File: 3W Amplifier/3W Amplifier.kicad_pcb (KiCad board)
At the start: 2 copper layers, 20 parts, among them SW1 SW_DIP_x02, U1 PAM8008

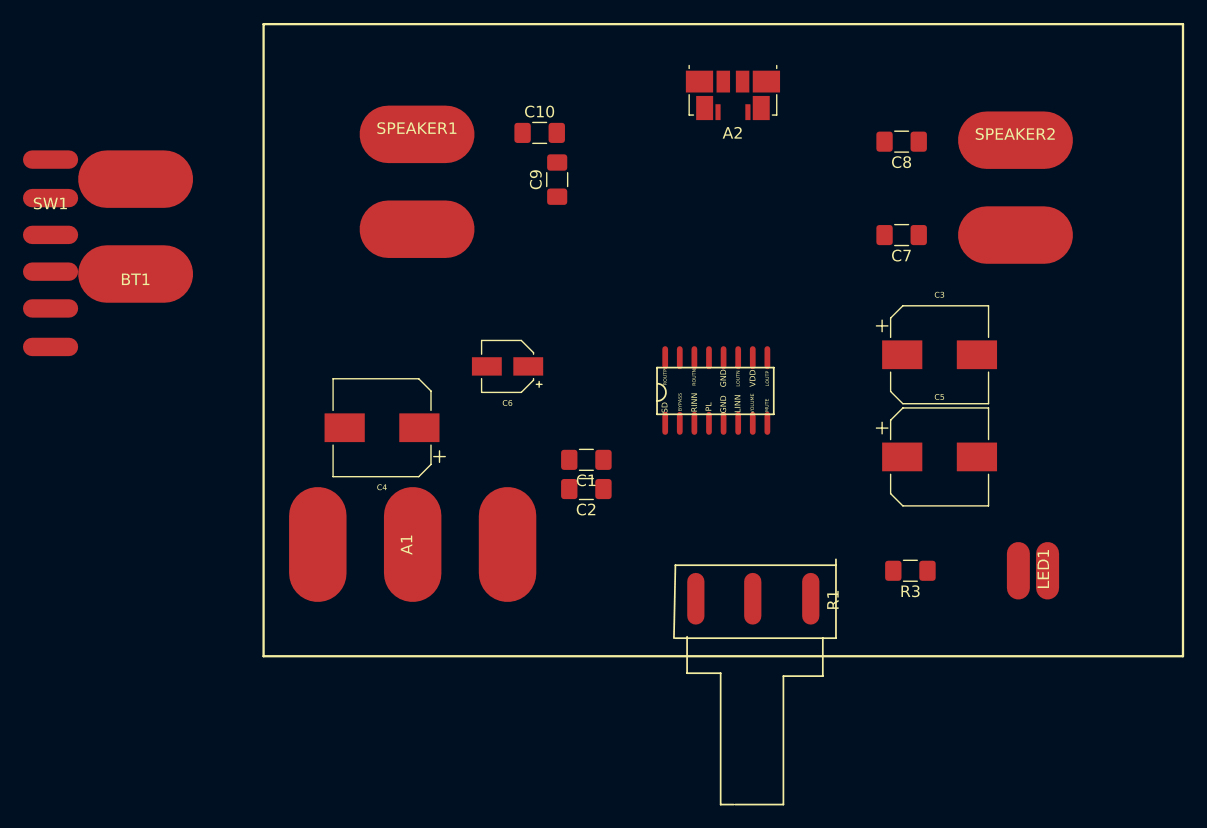
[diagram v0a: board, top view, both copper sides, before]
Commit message: everything routed but power
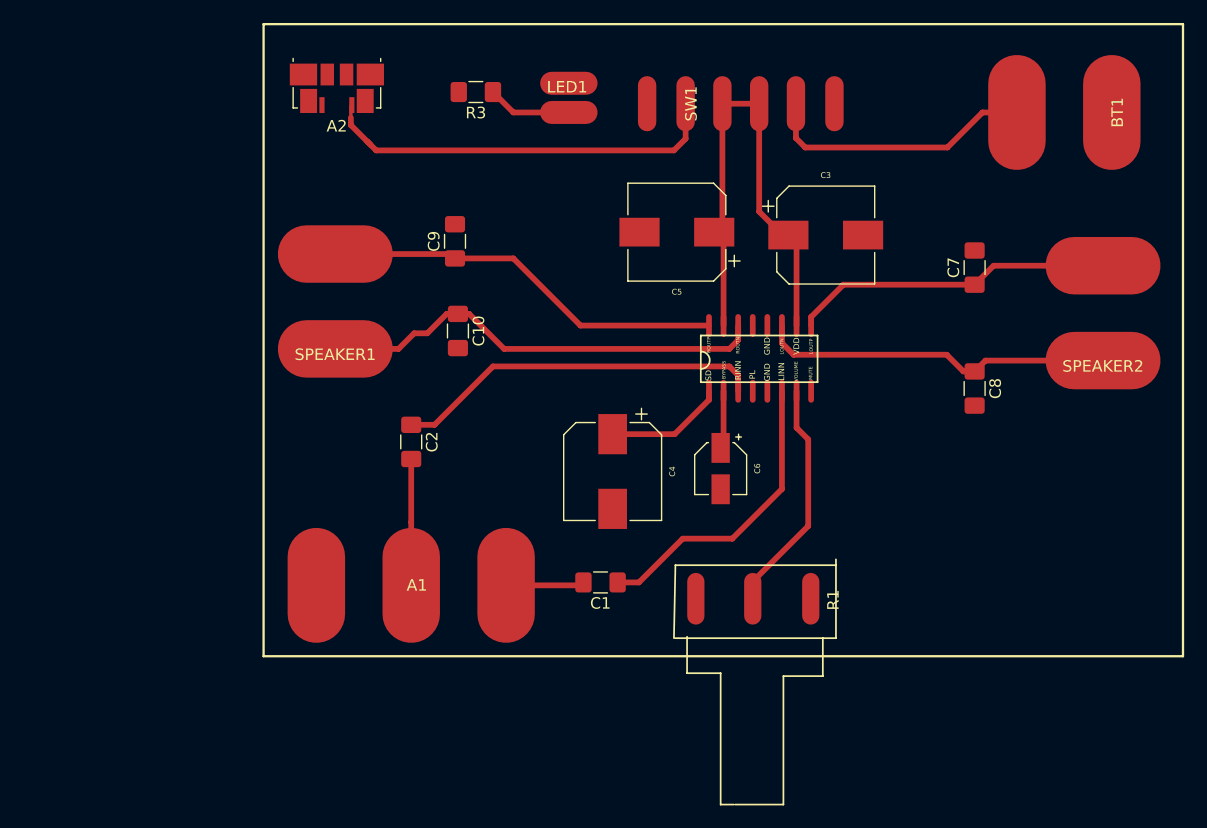
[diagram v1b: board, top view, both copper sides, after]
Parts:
- moved BT1 86.1 mm to (98.8, 27.7), turned to 90 degrees
- moved R3 56.3 mm to (43.5, 25.9)
- moved SW1 55.9 mm to (61.7, 26.9), turned to 90 degrees
- moved LED1 55.9 mm to (51.6, 27.7), turned to 0 degrees
- moved A2 34.5 mm to (31.4, 25.6)
- moved C5 30.1 mm to (61.0, 38.1), turned to 180 degrees
- moved C8 22.4 mm to (86.9, 51.7), turned to 270 degrees
- moved SPEAKER2 20.6 mm to (98.0, 49.3), turned to 0 degrees
- moved C6 20.6 mm to (64.8, 58.7), turned to 270 degrees
- moved C4 20.4 mm to (55.4, 58.9), turned to 270 degrees
- moved SPEAKER1 20.0 mm to (31.2, 48.3), turned to 0 degrees
- moved C10 18.6 mm to (41.9, 46.7), turned to 270 degrees
- moved C2 15.8 mm to (37.8, 56.4), turned to 270 degrees
- moved C3 14.4 mm to (73.9, 38.4)
- moved C1 10.7 mm to (54.3, 68.6)
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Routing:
- net /VDD: track 0.00 -> 54.4 mm
- net /ROUTN: track 0.00 -> 39.2 mm
- net (no net): track 0.00 -> 35.5 mm
- net /ROUTP: track 0.00 -> 35.1 mm
- net /RINN: track 0.00 -> 32.3 mm
- net /LOUTN: track 0.00 -> 30.9 mm
- net /LOUTP: track 0.00 -> 28.0 mm
- net /LINN: track 0.00 -> 26.2 mm
- net Net-(BT1-Pad1): track 0.00 -> 23.8 mm
- net /VOLUME: track 0.00 -> 20.5 mm
- net Net-(A1-PadR): track 0.00 -> 11.0 mm
- net Net-(LED1-Pad1): track 0.00 -> 7.34 mm
- net Net-(A1-PadT): track 0.00 -> 6.84 mm
- net /BYPASS: track 0.00 -> 5.04 mm

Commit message: add full GND pour
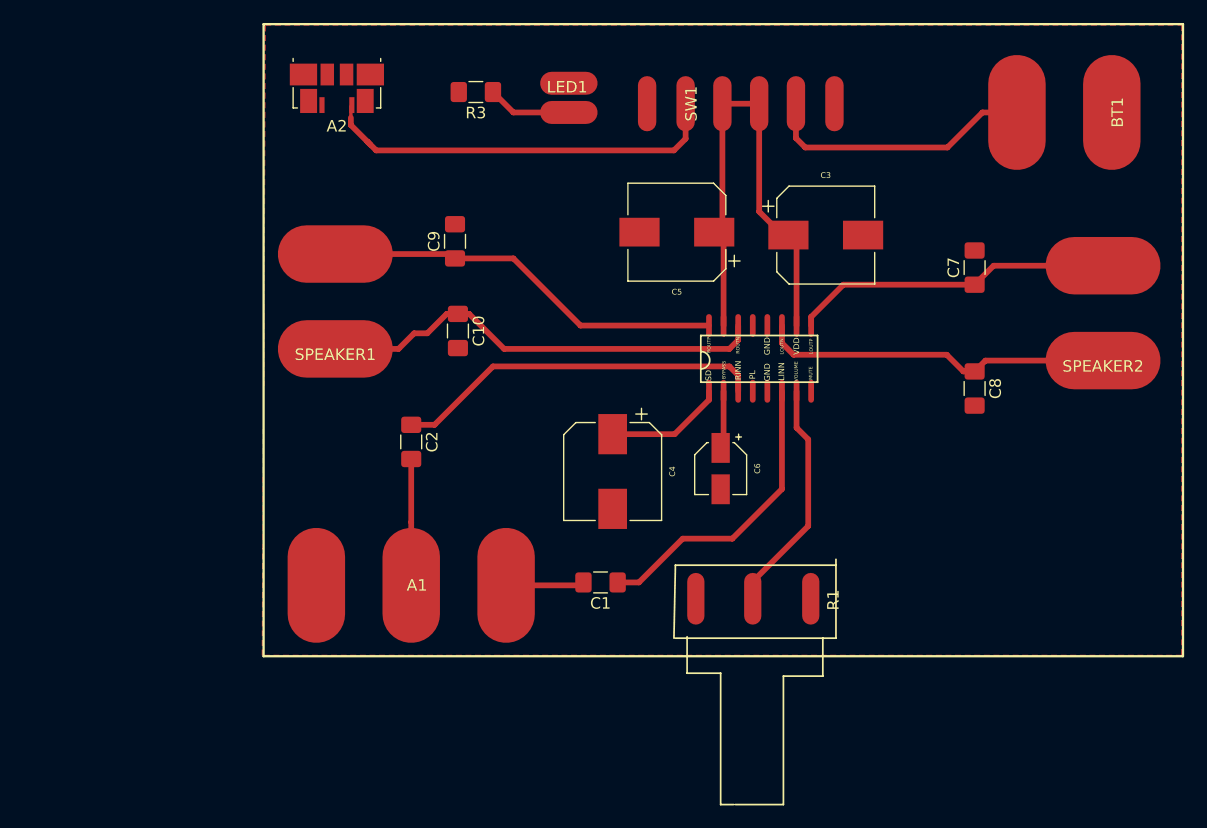
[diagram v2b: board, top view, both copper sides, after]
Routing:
- added copper zone on F.Cu, net /GND
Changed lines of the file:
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@@
   (segment (start 65.024 56.62) (end 64.77 56.874) (width 0.5) (layer F.Cu) (net 15))
   (segment (start 65.024 51.943) (end 65.024 56.62) (width 0.5) (layer F.Cu) (net 15))
+  (zone (net 3) (net_name /GND) (layer F.Cu) (hatch edge 0.508)
+    (connect_pads (clearance 0.508))
+    (min_thickness 0.254)
+    (fill yes (arc_segments 32) (thermal_gap 0.508) (thermal_bridge_width 0.508))
+    (polygon
+      (pts
+        (xy 25.146 20.066) (xy 104.902 20.066) (xy 104.902 74.93) (xy 24.892 74.93)
+      )
+    )
+  )
 )
